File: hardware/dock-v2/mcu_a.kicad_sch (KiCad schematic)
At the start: 29 parts, among them SW301 SW_Push, SW302 SW_Push, U301 RP2354A, Y301 12MHz

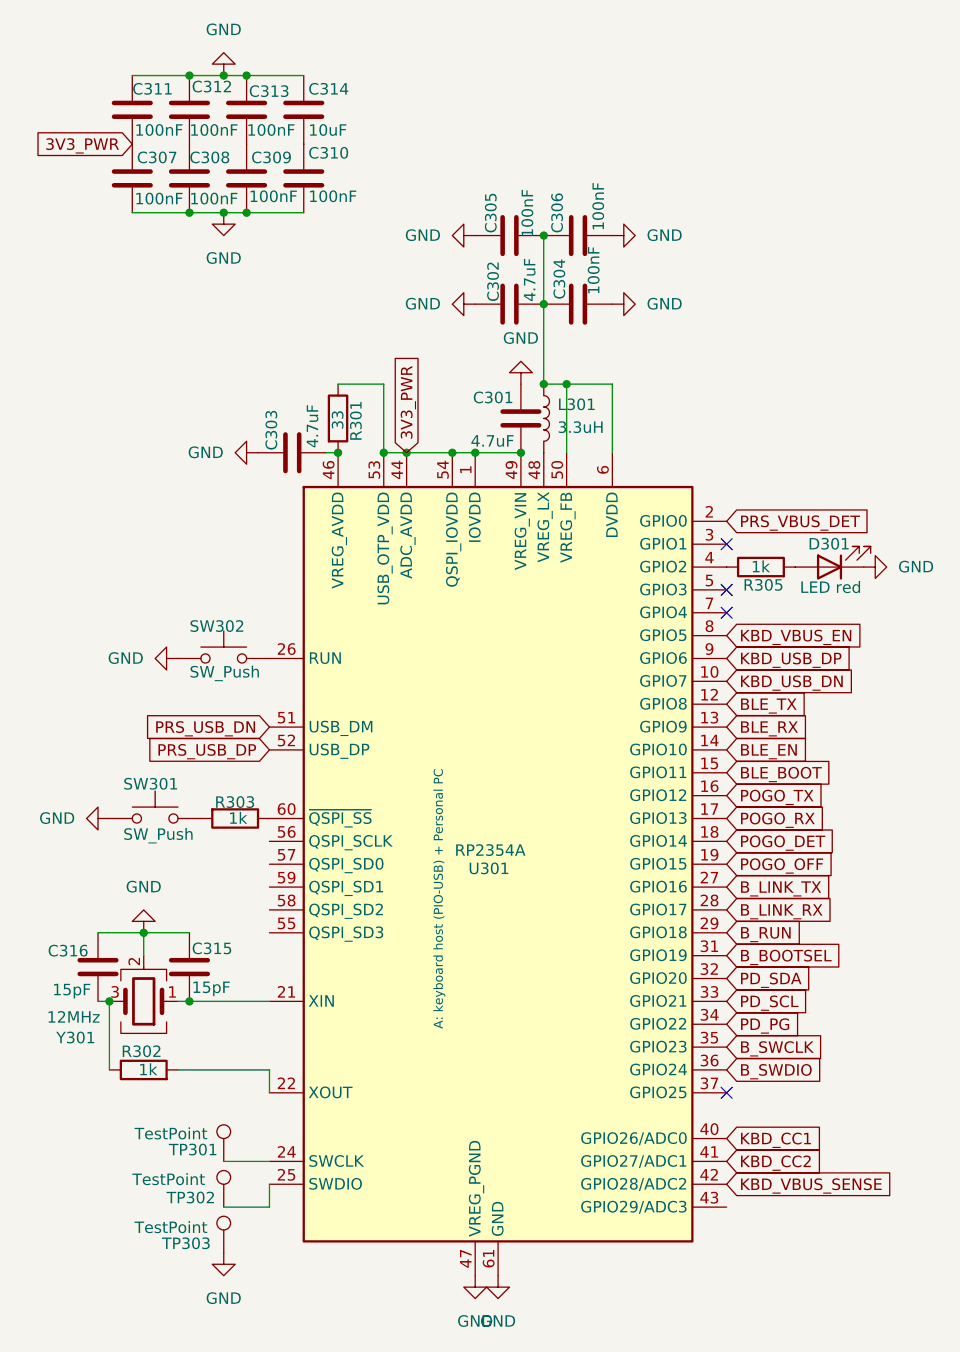
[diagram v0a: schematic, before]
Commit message: Dock v2 schematic: pogo sheet wired, fixes from review (user's work, snapshot)
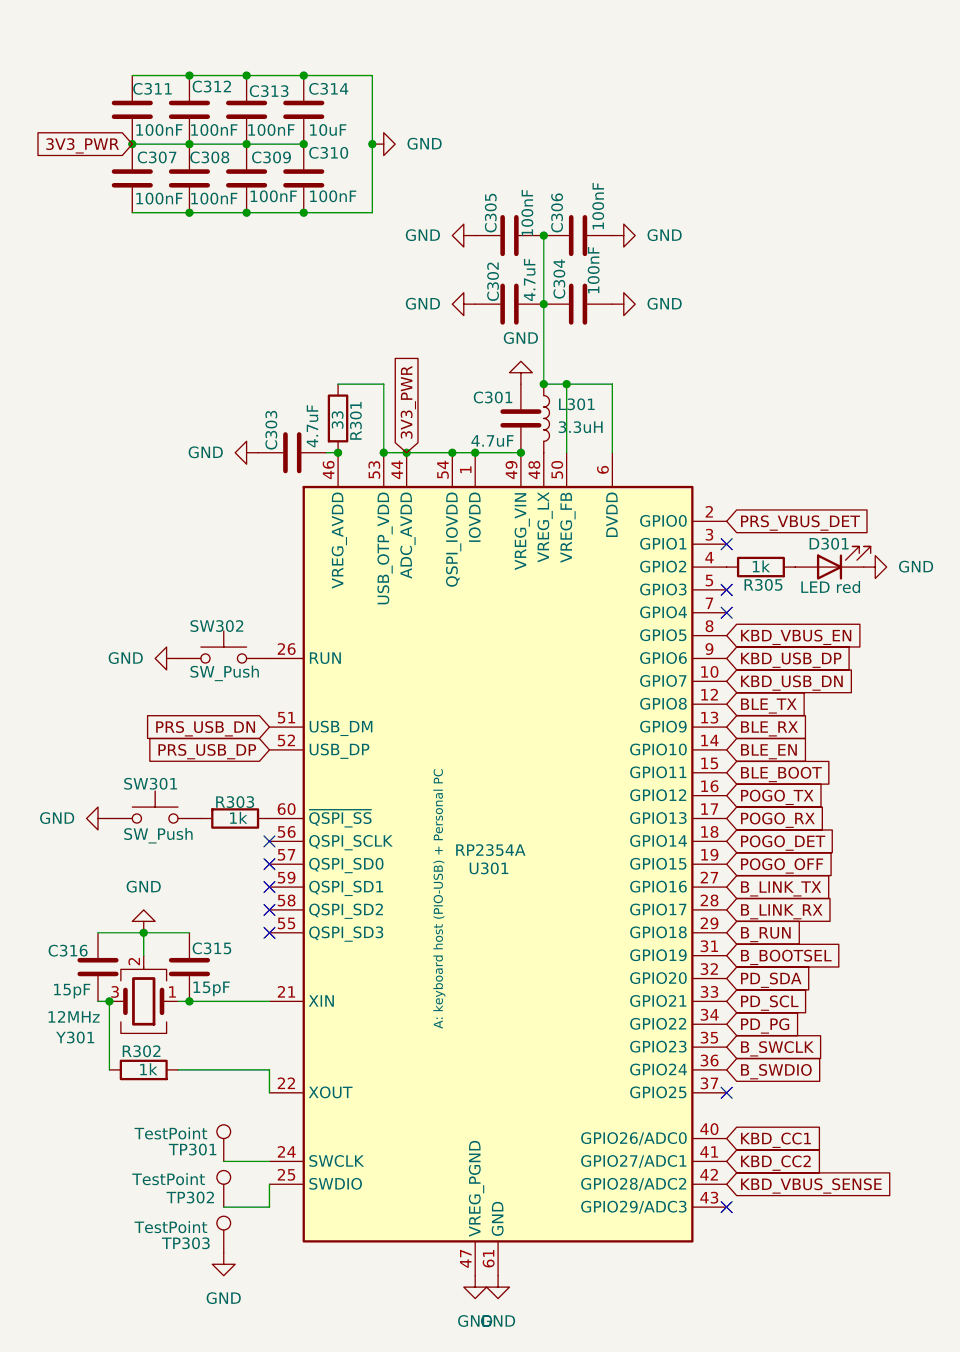
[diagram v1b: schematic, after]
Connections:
- net 3V3_PWR: now also C308.1, C309.1, C310.1, C312.2, C313.2, C314.2
- no-connect marks 4 -> 10
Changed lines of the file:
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@@
 	)
 	(junction
-		(at 153.67 46.99)
+		(at 156.21 39.37)
 		(diameter 0)
 		(color 0 0 0 0)
 	)
 	(junction
-		(at 181.61 73.66)
+		(at 149.86 39.37)
+		(diameter 0)
+		(color 0 0 0 0)
+	)
+	(junction
+		(at 143.51 39.37)
 		(diameter 0)
 		(color 0 0 0 0)
 	)
 	(junction
-		(at 153.67 31.75)
+		(at 162.56 46.99)
+		(diameter 0)
+		(color 0 0 0 0)
+	)
+	(junction
+		(at 181.61 73.66)
 		(diameter 0)
 		(color 0 0 0 0)
@@
 	)
 	(junction
+		(at 170.18 39.37)
+		(diameter 0)
+		(color 0 0 0 0)
+	)
+	(junction
+		(at 162.56 39.37)
+		(diameter 0)
+		(color 0 0 0 0)
+	)
+	(junction
 		(at 179.07 73.66)
 		(diameter 0)
@@
 	)
 	(junction
+		(at 162.56 31.75)
+		(diameter 0)
+		(color 0 0 0 0)
+	)
+	(junction
 		(at 149.86 31.75)
 		(diameter 0)
@@
 	)
 	(no_connect
+		(at 158.75 121.92)
+	)
+	(no_connect
 		(at 209.55 88.9)
 	)
@@
 	)
 	(no_connect
+		(at 158.75 127)
+	)
+	(no_connect
 		(at 209.55 83.82)
 	)
 	(no_connect
+		(at 158.75 119.38)
+	)
+	(no_connect
+		(at 209.55 157.48)
+	)
+	(no_connect
 		(at 209.55 91.44)
 	)
+	(no_connect
+		(at 158.75 124.46)
+	)
+	(no_connect
+		(at 158.75 116.84)
+	)
 	(wire
 		(pts
@@
 	(wire
 		(pts
-			(xy 149.86 46.99) (xy 153.67 46.99)
+			(xy 149.86 46.99) (xy 156.21 46.99)
 		)
 		(stroke
@@
 	(wire
 		(pts
+			(xy 149.86 39.37) (xy 156.21 39.37)
+		)
+		(stroke
+			(width 0)
+			(type default)
+		)
+	)
+	(wire
+		(pts
 			(xy 148.59 134.62) (xy 149.86 134.62)
 		)
@@
 	(wire
 		(pts
+			(xy 156.21 39.37) (xy 162.56 39.37)
+		)
+		(stroke
+			(width 0)
+			(type default)
+		)
+	)
+	(wire
+		(pts
 			(xy 191.77 66.04) (xy 196.85 66.04)
 		)
@@
 	(wire
 		(pts
-			(xy 153.67 46.99) (xy 156.21 46.99)
+			(xy 165.1 73.66) (xy 166.37 73.66)
 		)
 		(stroke
@@
 	(wire
 		(pts
-			(xy 165.1 73.66) (xy 166.37 73.66)
+			(xy 158.75 142.24) (xy 158.75 144.78)
 		)
 		(stroke
@@
 	(wire
 		(pts
-			(xy 158.75 142.24) (xy 158.75 144.78)
+			(xy 156.21 46.99) (xy 162.56 46.99)
 		)
 		(stroke
@@
 	(wire
 		(pts
-			(xy 156.21 46.99) (xy 162.56 46.99)
+			(xy 170.18 39.37) (xy 170.18 31.75)
+		)
+		(stroke
+			(width 0)
+			(type default)
+		)
+	)
+	(wire
+		(pts
+			(xy 162.56 46.99) (xy 170.18 46.99)
 		)
 		(stroke
@@
 	(wire
 		(pts
+			(xy 143.51 39.37) (xy 149.86 39.37)
+		)
+		(stroke
+			(width 0)
+			(type default)
+		)
+	)
+	(wire
+		(pts
 			(xy 189.23 66.04) (xy 191.77 66.04)
 		)
@@
 	(wire
 		(pts
-			(xy 149.86 31.75) (xy 153.67 31.75)
+			(xy 149.86 31.75) (xy 156.21 31.75)
 		)
 		(stroke
@@
 	(wire
 		(pts
-			(xy 153.67 31.75) (xy 156.21 31.75)
+			(xy 170.18 31.75) (xy 162.56 31.75)
 		)
 		(stroke
@@
 	(wire
 		(pts
+			(xy 170.18 46.99) (xy 170.18 39.37)
+		)
+		(stroke
+			(width 0)
+			(type default)
+		)
+	)
+	(wire
+		(pts
 			(xy 189.23 49.53) (xy 189.23 57.15)
 		)
@@
 	(symbol
 		(lib_id "power:GND")
+		(at 170.18 39.37 90)
+		(unit 1)
+		(body_style 1)
+		(exclude_from_sim no)
+		(in_bom yes)
+		(on_board yes)
+		(in_pos_files yes)
+		(dnp no)
+		(fields_autoplaced yes)
+		(property "Reference" "#PWR0409"
+			(at 176.53 39.37 0)
+			(hide yes)
+			(show_name no)
+			(do_not_autoplace no)
+			(effects
+				(font
+					(size 1.27 1.27)
+				)
+			)
+		)
+		(property "Value" "GND"
+			(at 173.99 39.3699 90)
+			(show_name no)
+			(do_not_autoplace no)
+			(effects
+				(font
+					(size 1.27 1.27)
+				)
+				(justify right)
+			)
+		)
+		(property "Footprint" ""
+			(at 170.18 39.37 0)
+			(hide yes)
+			(show_name no)
+			(do_not_autoplace no)
+			(effects
+				(font
+					(size 1.27 1.27)
+				)
+			)
+		)
+		(property "Datasheet" ""
+			(at 170.18 39.37 0)
+			(hide yes)
+			(show_name no)
+			(do_not_autoplace no)
+			(effects
+				(font
+					(size 1.27 1.27)
+				)
+			)
+		)
+		(property "Description" "Power symbol creates a global label with name \"GND\" , ground"
+			(at 170.18 39.37 0)
+			(hide yes)
+			(show_name no)
+			(do_not_autoplace no)
+			(effects
+				(font
+					(size 1.27 1.27)
+				)
+			)
+		)
+		(pin "1"
+		)
+		(instances
+			(project "dock-v2"
+				(path "/928a9dc6-b0ce-4f47-a17d-f26fd77e396a/bcfba91e-3181-4d07-9970-4b16b455c32a"
+					(reference "#PWR0409")
+					(unit 1)
+				)
+			)
+		)
+	)
+	(symbol
+		(lib_id "power:GND")
 		(at 196.85 57.15 90)
 		(unit 1)
@@
 	)
 	(symbol
-		(lib_id "power:GND")
-		(at 153.67 46.99 0)
-		(unit 1)
-		(body_style 1)
-		(exclude_from_sim no)
-		(in_bom yes)
-		(on_board yes)
-		(in_pos_files yes)
-		(dnp no)
-		(fields_autoplaced yes)
-		(property "Reference" "#PWR0409"
-			(at 153.67 53.34 0)
-			(hide yes)
-			(show_name no)
-			(do_not_autoplace no)
-			(effects
-				(font
-					(size 1.27 1.27)
-				)
-			)
-		)
-		(property "Value" "GND"
-			(at 153.67 52.07 0)
-			(show_name no)
-			(do_not_autoplace no)
-			(effects
-				(font
-					(size 1.27 1.27)
-				)
-			)
-		)
-		(property "Footprint" ""
-			(at 153.67 46.99 0)
-			(hide yes)
-			(show_name no)
-			(do_not_autoplace no)
-			(effects
-				(font
-					(size 1.27 1.27)
-				)
-			)
-		)
-		(property "Datasheet" ""
-			(at 153.67 46.99 0)
-			(hide yes)
-			(show_name no)
-			(do_not_autoplace no)
-			(effects
-				(font
-					(size 1.27 1.27)
-				)
-			)
-		)
-		(property "Description" "Power symbol creates a global label with name \"GND\" , ground"
-			(at 153.67 46.99 0)
-			(hide yes)
-			(show_name no)
-			(do_not_autoplace no)
-			(effects
-				(font
-					(size 1.27 1.27)
-				)
-			)
-		)
-		(pin "1"
-		)
-		(instances
-			(project "dock-v2"
-				(path "/928a9dc6-b0ce-4f47-a17d-f26fd77e396a/bcfba91e-3181-4d07-9970-4b16b455c32a"
-					(reference "#PWR0409")
-					(unit 1)
-				)
-			)
-		)
-	)
-	(symbol
 		(lib_id "Connector:TestPoint")
 		(at 153.67 157.48 0)
@@
 					(unit 1)
 				)
-			)
-		)
-	)
-	(symbol
-		(lib_id "power:GND")
-		(at 153.67 31.75 180)
-		(unit 1)
-		(body_style 1)
-		(exclude_from_sim no)
-		(in_bom yes)
-		(on_board yes)
-		(in_pos_files yes)
-		(dnp no)
-		(fields_autoplaced yes)
-		(property "Reference" "#PWR0410"
-			(at 153.67 25.4 0)
-			(hide yes)
-			(show_name no)
-			(do_not_autoplace no)
-			(effects
-				(font
-					(size 1.27 1.27)
-				)
-			)
-		)
-		(property "Value" "GND"
-			(at 153.67 26.67 0)
-			(show_name no)
-			(do_not_autoplace no)
-			(effects
-				(font
-					(size 1.27 1.27)
-				)
-			)
-		)
-		(property "Footprint" ""
-			(at 153.67 31.75 0)
-			(hide yes)
-			(show_name no)
-			(do_not_autoplace no)
-			(effects
-				(font
-					(size 1.27 1.27)
-				)
-			)
-		)
-		(property "Datasheet" ""
-			(at 153.67 31.75 0)
-			(hide yes)
-			(show_name no)
-			(do_not_autoplace no)
-			(effects
-				(font
-					(size 1.27 1.27)
-				)
-			)
-		)
-		(property "Description" "Power symbol creates a global label with name \"GND\" , ground"
-			(at 153.67 31.75 0)
-			(hide yes)
-			(show_name no)
-			(do_not_autoplace no)
-			(effects
-				(font
-					(size 1.27 1.27)
-				)
-			)
-		)
-		(pin "1"
-		)
-		(instances
-			(project "dock-v2"
-				(path "/928a9dc6-b0ce-4f47-a17d-f26fd77e396a/bcfba91e-3181-4d07-9970-4b16b455c32a"
-					(reference "#PWR0410")
-					(unit 1)
-				)

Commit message: Dock v2 schematic: user's fixes (snapshot)
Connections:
- net POGO_5V_SENSE: now reaches U301.43 (GPIO29/ADC3)
- no-connect marks 10 -> 9
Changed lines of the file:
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@@
-	)
-	(no_connect
-		(at 209.55 157.48)
 	)
 	(no_connect
@@
 			(hide yes)
 			(show_name no)
+			(do_not_autoplace no)
+			(effects
+				(font
+					(size 1.27 1.27)
+				)
+				(justify left)
+			)
+		)
+	)
+	(global_label "POGO_5V_SENSE"
+		(shape input)
+		(at 209.55 157.48 0)
+		(fields_autoplaced yes)
+		(effects
+			(font
+				(size 1.27 1.27)
+			)
+			(justify left)
+		)
+		(property "Intersheetrefs" "${INTERSHEET_REFS}"
+			(at 228.017 157.48 0)
+			(hide yes)
+			(show_name no)
